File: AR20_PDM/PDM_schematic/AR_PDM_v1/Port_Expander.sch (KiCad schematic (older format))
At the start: 5 parts, among them U9 TCA6424ARGJR

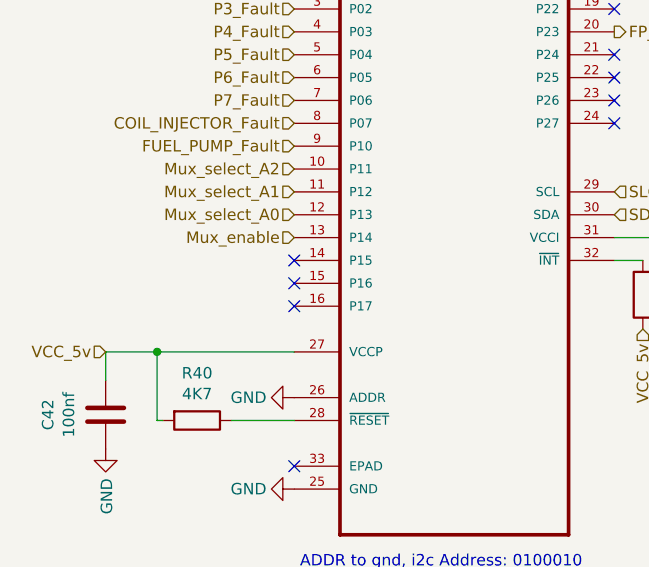
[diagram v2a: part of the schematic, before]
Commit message: Further testing, reveals pdm needs rework
-  As of now, there are major errors in schematics.
- Needs rework. Version charlie postponed.
- Very nice pcb layout thats almost finished. 
   worth noting this layout for the future
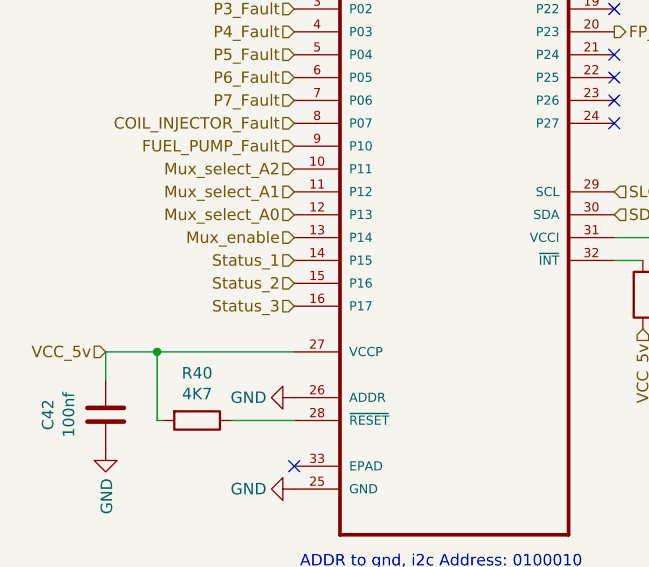
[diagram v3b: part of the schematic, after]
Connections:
- net Status_1: now reaches U9.14 (P15)
- net Status_2: now reaches U9.15 (P16)
- net Status_3: now reaches U9.16 (P17)
- no-connect marks 11 -> 8
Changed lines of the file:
@@
 	0    1    1    0
 $EndComp
+Text HLabel 6475 2950 2    50   Output ~ 0
+FP_ENABLE_ACM
+NoConn ~ 6475 2850
+NoConn ~ 6475 3050
+NoConn ~ 6475 3250
+NoConn ~ 6475 3150
+NoConn ~ 6475 3350
+Text HLabel 5075 3750 0    50   Input ~ 0
+Mux_select_A0
+Text HLabel 5075 3650 0    50   Input ~ 0
+Mux_select_A1
+Text HLabel 5075 3550 0    50   Input ~ 0
+Mux_select_A2
+Text HLabel 5075 3850 0    50   Input ~ 0
+Mux_enable
+Text HLabel 5075 3350 0    50   Input ~ 0
+COIL_INJECTOR_Fault
+Text HLabel 5075 3450 0    50   Input ~ 0
+FUEL_PUMP_Fault
+NoConn ~ 6475 2750
+NoConn ~ 6475 2650
+Text HLabel 5075 4050 0    50   Input ~ 0
+Status_2
+Text HLabel 5075 3950 0    50   Input ~ 0
+Status_1
+Text HLabel 5075 4150 0    50   Input ~ 0
+Status_3
 $Comp
 L AR20_PDM_v1-rescue:TCA6424ARGJR U9
@@
 	1    0    0    -1
 $EndComp
-Text HLabel 6475 2950 2    50   Output ~ 0
-FP_ENABLE_ACM
-NoConn ~ 6475 2850
-NoConn ~ 6475 3050
-NoConn ~ 6475 3250
-NoConn ~ 6475 3150
-NoConn ~ 6475 3350
-Text HLabel 5075 3750 0    50   Input ~ 0
-Mux_select_A0
-Text HLabel 5075 3650 0    50   Input ~ 0
-Mux_select_A1
-Text HLabel 5075 3550 0    50   Input ~ 0
-Mux_select_A2
-Text HLabel 5075 3850 0    50   Input ~ 0
-Mux_enable
-NoConn ~ 5075 3950
-NoConn ~ 5075 4050
-NoConn ~ 5075 4150
-Text HLabel 5075 3350 0    50   Input ~ 0
-COIL_INJECTOR_Fault
-Text HLabel 5075 3450 0    50   Input ~ 0
-FUEL_PUMP_Fault
-NoConn ~ 6475 2750
-NoConn ~ 6475 2650
 $EndSCHEMATC

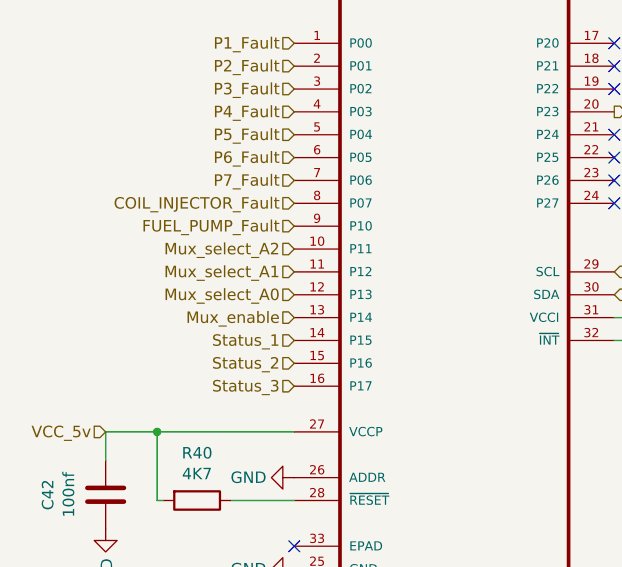
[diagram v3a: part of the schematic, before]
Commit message: schematics rework
Fixed INA233 frying due to inductive flyback:
- Paced ina233 high side of the mosftets
- New input protection reseistors, and zener diodes, on each ina233.
Simplified:
- Removed the MUX and mos sense lines, as i realize that most of this functionality can be obtained trough INA233.
- Removed some of the cappacitors , besides the most needed ones.
- removed  back to back zener diode configuration, now a single diode insted.
 to reduce negative voltage in case of loss of VS, to be easy on the INA233 filters.
new stuff:
- Another temp sensor.
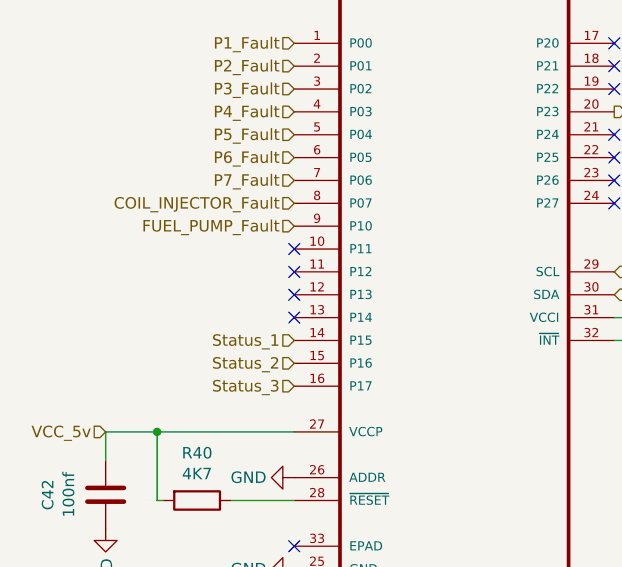
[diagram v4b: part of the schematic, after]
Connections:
- net Mux_enable: no longer names the net of U9.13 (P14)
- net Mux_select_A0: no longer names the net of U9.12 (P13)
- net Mux_select_A1: no longer names the net of U9.11 (P12)
- net Mux_select_A2: no longer names the net of U9.10 (P11)
- no-connect marks 8 -> 12
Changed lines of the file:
@@
 $Descr A4 11693 8268
 encoding utf-8
-Sheet 14 14
+Sheet 13 13
 Title ""
 Date ""
@@
 NoConn ~ 6475 3150
 NoConn ~ 6475 3350
-Text HLabel 5075 3750 0    50   Input ~ 0
-Mux_select_A0
-Text HLabel 5075 3650 0    50   Input ~ 0
-Mux_select_A1
-Text HLabel 5075 3550 0    50   Input ~ 0
-Mux_select_A2
-Text HLabel 5075 3850 0    50   Input ~ 0
-Mux_enable
 Text HLabel 5075 3350 0    50   Input ~ 0
 COIL_INJECTOR_Fault
@@
 	1    0    0    -1
 $EndComp
+NoConn ~ 5075 3550
+NoConn ~ 5075 3650
+NoConn ~ 5075 3750
+NoConn ~ 5075 3850
 $EndSCHEMATC

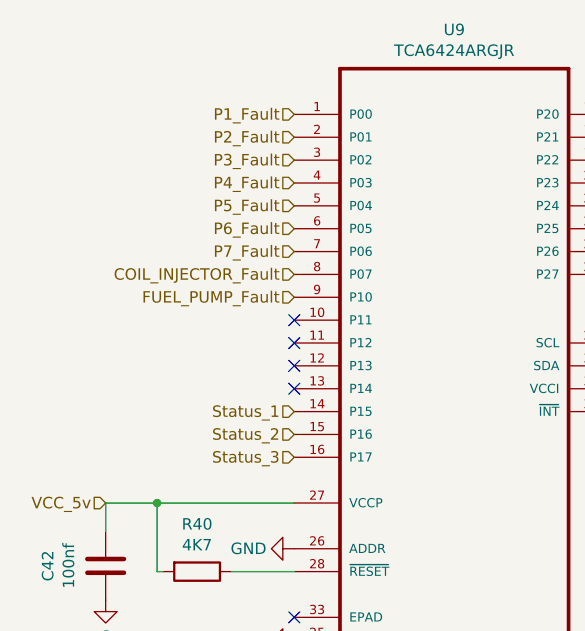
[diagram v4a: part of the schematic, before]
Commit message: PDM mostly complete
- Reverse polarity protection implemented
- All traces layed out
- final polish missing
- DRC missing
- Final check missing
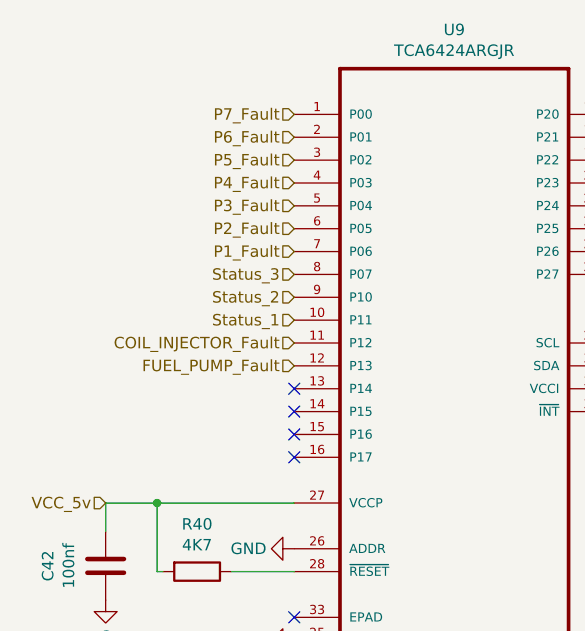
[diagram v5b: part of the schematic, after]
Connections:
- net COIL_INJECTOR_Fault: now also U9.11 (P12); no longer U9.8 (P07)
- net FUEL_PUMP_Fault: now also U9.12 (P13); no longer U9.9 (P10)
- net P1_Fault: now also U9.7 (P06); no longer U9.1 (P00)
- net P2_Fault: now also U9.6 (P05); no longer U9.2 (P01)
- net P3_Fault: now also U9.5 (P04); no longer U9.3 (P02)
- net P5_Fault: now also U9.3 (P02); no longer U9.5 (P04)
- net P6_Fault: now also U9.2 (P01); no longer U9.6 (P05)
- net P7_Fault: now also U9.1 (P00); no longer U9.7 (P06)
- net Status_1: now also U9.10 (P11); no longer U9.14 (P15)
- net Status_2: now also U9.9 (P10); no longer U9.15 (P16)
- net Status_3: now also U9.8 (P07); no longer U9.16 (P17)
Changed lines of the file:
@@
 	0    1    1    0
 $EndComp
-Text HLabel 5075 3250 0    50   Input ~ 0
+Text HLabel 5075 2650 0    50   Input ~ 0
 P7_Fault
-Text HLabel 5075 3150 0    50   Input ~ 0
+Text HLabel 5075 2750 0    50   Input ~ 0
 P6_Fault
-Text HLabel 5075 3050 0    50   Input ~ 0
+Text HLabel 5075 2850 0    50   Input ~ 0
 P5_Fault
 Text HLabel 5075 2950 0    50   Input ~ 0
 P4_Fault
-Text HLabel 5075 2850 0    50   Input ~ 0
+Text HLabel 5075 3050 0    50   Input ~ 0
 P3_Fault
-Text HLabel 5075 2650 0    50   Input ~ 0
+Text HLabel 5075 3250 0    50   Input ~ 0
 P1_Fault
-Text HLabel 5075 2750 0    50   Input ~ 0
+Text HLabel 5075 3150 0    50   Input ~ 0
 P2_Fault
 NoConn ~ 5075 4850
@@
 NoConn ~ 6475 3150
 NoConn ~ 6475 3350
-Text HLabel 5075 3350 0    50   Input ~ 0
-COIL_INJECTOR_Fault
-Text HLabel 5075 3450 0    50   Input ~ 0
-FUEL_PUMP_Fault
 NoConn ~ 6475 2750
 NoConn ~ 6475 2650
-Text HLabel 5075 4050 0    50   Input ~ 0
+Text HLabel 5075 3450 0    50   Input ~ 0
 Status_2
-Text HLabel 5075 3950 0    50   Input ~ 0
+Text HLabel 5075 3550 0    50   Input ~ 0
 Status_1
-Text HLabel 5075 4150 0    50   Input ~ 0
+Text HLabel 5075 3350 0    50   Input ~ 0
 Status_3
+NoConn ~ 5075 3950
+NoConn ~ 5075 3850
+NoConn ~ 5075 4150
+Text HLabel 5075 3750 0    50   Input ~ 0
+FUEL_PUMP_Fault
+Text HLabel 5075 3650 0    50   Input ~ 0
+COIL_INJECTOR_Fault
 $Comp
 L AR20_PDM_v1-rescue:TCA6424ARGJR U9
@@
 	1    0    0    -1
 $EndComp
-NoConn ~ 5075 3550
-NoConn ~ 5075 3650
-NoConn ~ 5075 3750
-NoConn ~ 5075 3850
+NoConn ~ 5075 4050
 $EndSCHEMATC

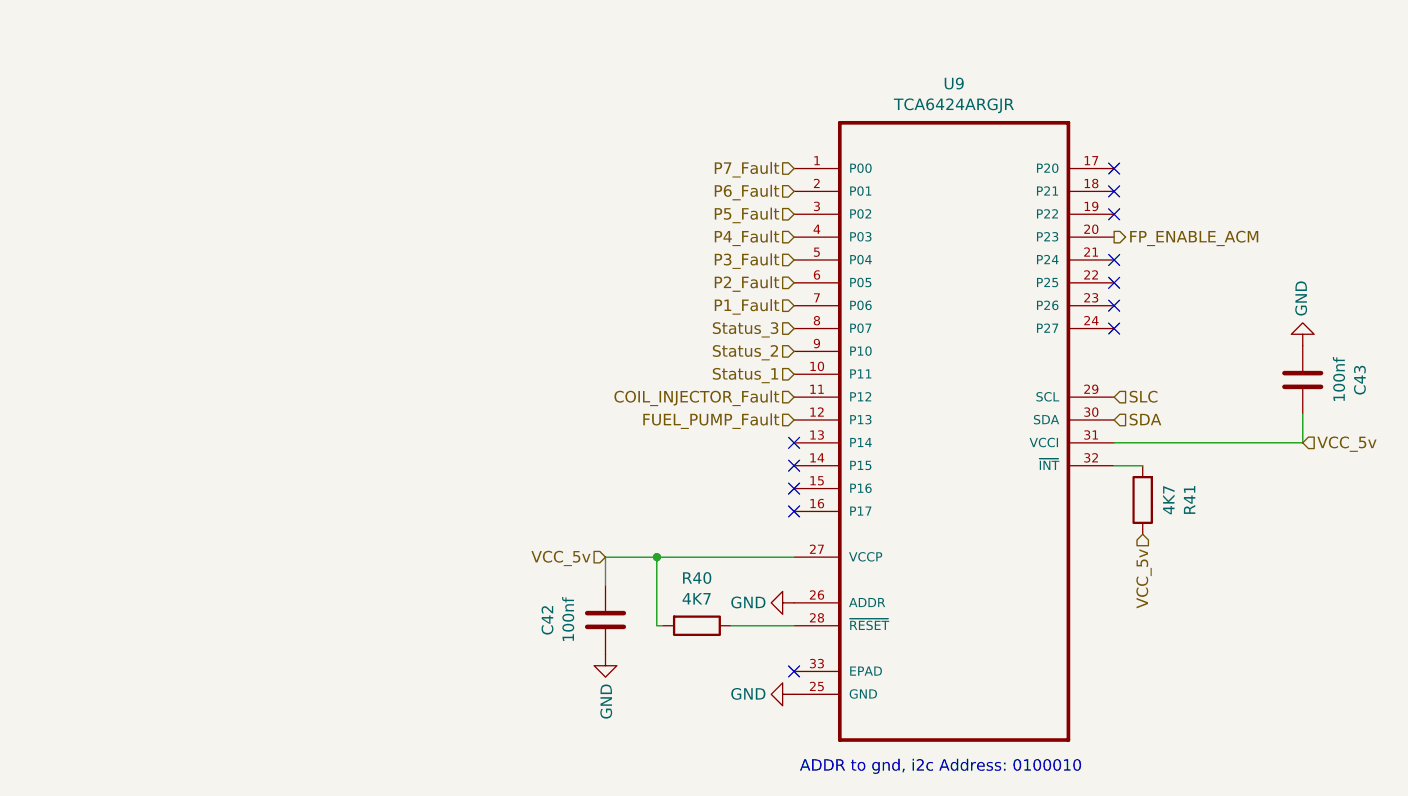
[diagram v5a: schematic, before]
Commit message: Added shutdown circuit monitoring, new gerber files
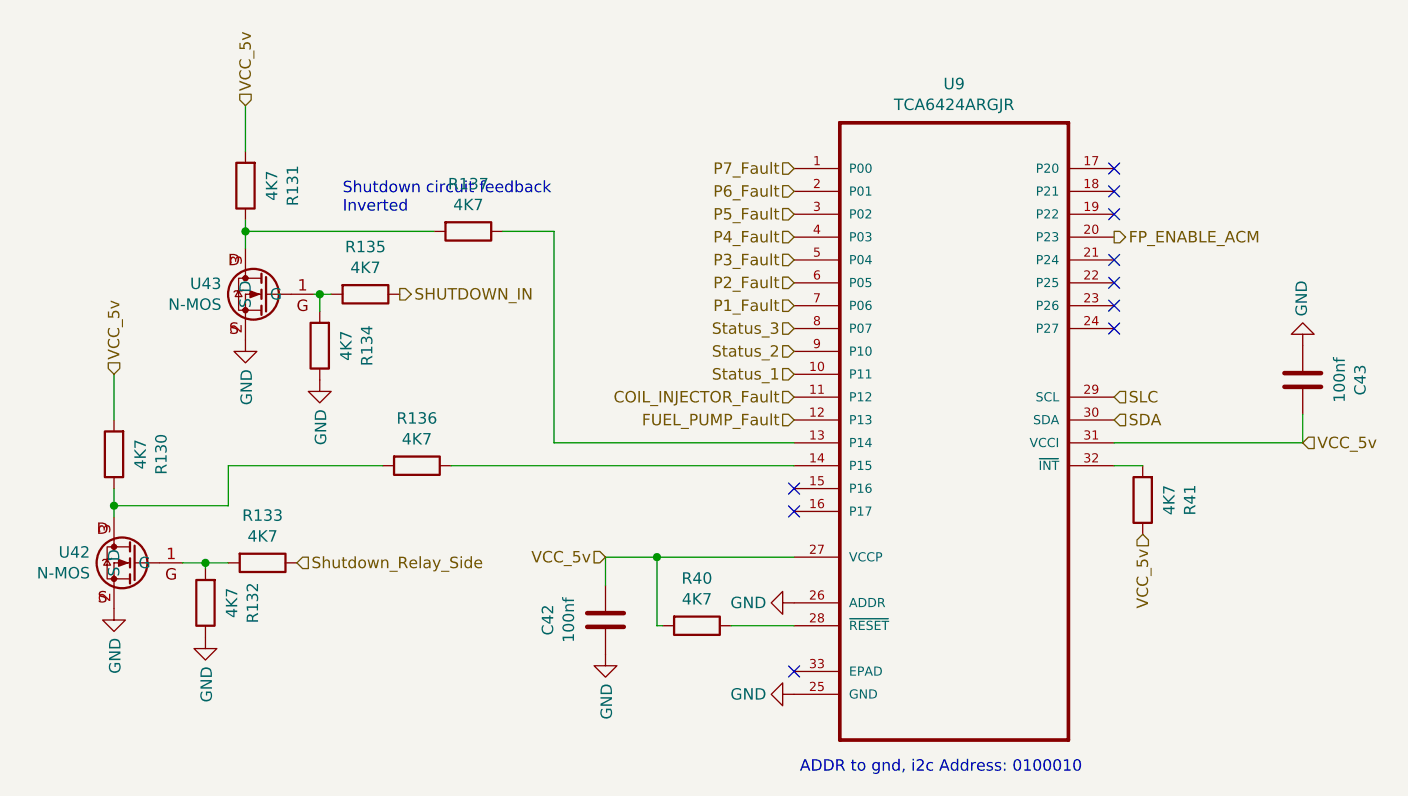
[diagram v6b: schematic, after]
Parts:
- added R130, R131, R132, R133, R134, R135, R136, R137: 4K7, Resistor_SMD:R_0603_1608Metric, symbol AR20_PDM_v1-rescue:R-Device
- added U42, U43: N-MOS, AR_PDM_v1:N-MOS-DMN6140L-13, symbol AR20_PDM_v1-rescue:N-MOS-DMN6140L-13
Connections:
- net GND: now also R132.1, R134.1, U42.2 (S), U43.2 (S)
- net VCC_5v: now also R130.2, R131.2
- net at U9.13 (P14): now also R137.1
- net at U9.14 (P15): now also R136.1
- new net: R132.2, R133.2, U42.1 (G)
- new net: R130.1, R136.2, U42.3 (D)
- new net: R134.2, R135.2, U43.1 (G)
- new net: R131.1, R137.2, U43.3 (D)
- new net SHUTDOWN_IN: R135.1
- new net Shutdown_Relay_Side: R133.1
- no-connect marks 12 -> 10
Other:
- note added: "Shutdown circuit feedback\nInverted"

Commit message: A litte fix in the shutdown monitoring, new gerber files
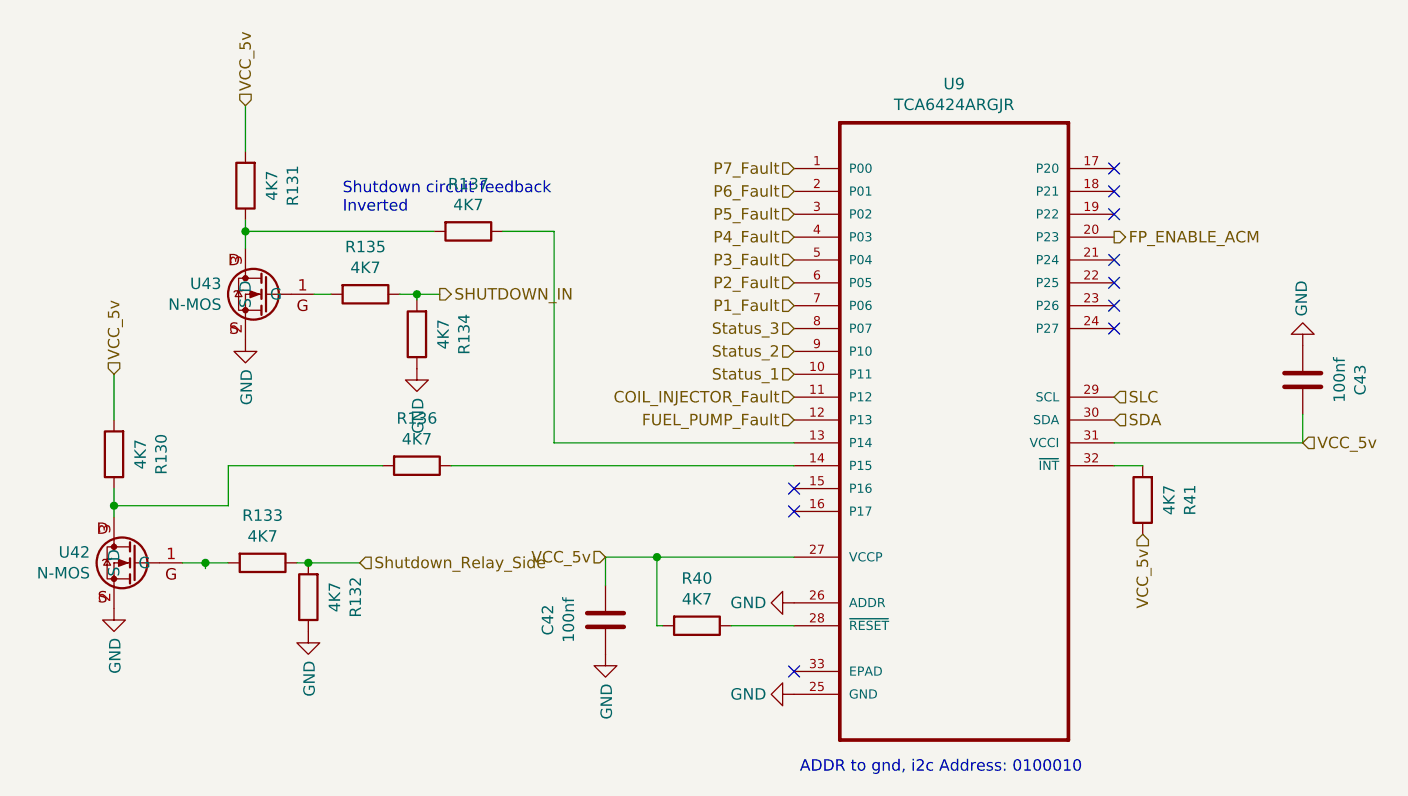
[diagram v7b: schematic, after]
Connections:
- wire segments 29 -> 32
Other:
- moved on the sheet: R132, R134
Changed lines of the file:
@@
 L AR20_PDM_v1-rescue:R-Device R?
 U 1 1 5F452FFA
-P 3000 3425
+P 3425 3375
 AR Path="/5DA89415/5F452FFA" Ref="R?"  Part="1"
 AR Path="/5DA8920B/5F452FFA" Ref="R?"  Part="1"
 AR Path="/5E2546F2/5F452FFA" Ref="R?"  Part="1"
 AR Path="/5E1AEC18/5F452FFA" Ref="R134"  Part="1"
-F 0 "R134" V 2793 3425 50  0000 C CNN
-F 1 "4K7" V 2884 3425 50  0000 C CNN
-F 2 "Resistor_SMD:R_0603_1608Metric" V 2930 3425 50  0001 C CNN
-F 3 "~" H 3000 3425 50  0001 C CNN
-	1    3000 3425
+F 0 "R134" V 3218 3375 50  0000 C CNN
+F 1 "4K7" V 3309 3375 50  0000 C CNN
+F 2 "Resistor_SMD:R_0603_1608Metric" V 3355 3375 50  0001 C CNN
+F 3 "~" H 3425 3375 50  0001 C CNN
+	1    3425 3375
 	-1   0    0    1
 $EndComp
@@
 	4025 3850 4025 2925
 Wire Wire Line
-	3050 3200 3000 3200
-Wire Wire Line
-	3000 3275 3000 3200
-Connection ~ 3000 3200
-Wire Wire Line
-	3000 3200 2975 3200
-Wire Wire Line
 	2100 4125 2100 4175
 Wire Wire Line
@@
 L AR20_PDM_v1-rescue:R-Device R?
 U 1 1 5F461877
-P 2500 4550
+P 2950 4525
 AR Path="/5DA89415/5F461877" Ref="R?"  Part="1"
 AR Path="/5DA8920B/5F461877" Ref="R?"  Part="1"
 AR Path="/5E2546F2/5F461877" Ref="R?"  Part="1"
 AR Path="/5E1AEC18/5F461877" Ref="R132"  Part="1"
-F 0 "R132" V 2293 4550 50  0000 C CNN
-F 1 "4K7" V 2384 4550 50  0000 C CNN
-F 2 "Resistor_SMD:R_0603_1608Metric" V 2430 4550 50  0001 C CNN
-F 3 "~" H 2500 4550 50  0001 C CNN
-	1    2500 4550
+F 0 "R132" V 2743 4525 50  0000 C CNN
+F 1 "4K7" V 2834 4525 50  0000 C CNN
+F 2 "Resistor_SMD:R_0603_1608Metric" V 2880 4525 50  0001 C CNN
+F 3 "~" H 2950 4525 50  0001 C CNN
+	1    2950 4525
 	-1   0    0    1
 $EndComp
@@
 L AR20_PDM_v1-rescue:GND-power #PWR?
 U 1 1 5F45F5EF
-P 3000 3575
+P 3425 3525
 AR Path="/5DA89415/5F45F5EF" Ref="#PWR?"  Part="1"
 AR Path="/5DEB10A1/5F45F5EF" Ref="#PWR?"  Part="1"
@@
 AR Path="/5E10174B/5F45F5EF" Ref="#PWR?"  Part="1"
 AR Path="/5E1AEC18/5F45F5EF" Ref="#PWR0172"  Part="1"
-F 0 "#PWR0172" H 3000 3325 50  0001 C CNN
-F 1 "GND" V 3005 3447 50  0000 R CNN
-F 2 "" H 3000 3575 50  0001 C CNN
-F 3 "" H 3000 3575 50  0001 C CNN
-	1    3000 3575
+F 0 "#PWR0172" H 3425 3275 50  0001 C CNN
+F 1 "GND" V 3430 3397 50  0000 R CNN
+F 2 "" H 3425 3525 50  0001 C CNN
+F 3 "" H 3425 3525 50  0001 C CNN
+	1    3425 3525
 	1    0    0    -1
 $EndComp
@@
 L AR20_PDM_v1-rescue:GND-power #PWR?
 U 1 1 5F4625C1
-P 2500 4700
+P 2950 4675
 AR Path="/5DA89415/5F4625C1" Ref="#PWR?"  Part="1"
 AR Path="/5DEB10A1/5F4625C1" Ref="#PWR?"  Part="1"
@@
 AR Path="/5E10174B/5F4625C1" Ref="#PWR?"  Part="1"
 AR Path="/5E1AEC18/5F4625C1" Ref="#PWR0173"  Part="1"
-F 0 "#PWR0173" H 2500 4450 50  0001 C CNN
-F 1 "GND" V 2505 4572 50  0000 R CNN
-F 2 "" H 2500 4700 50  0001 C CNN
-F 3 "" H 2500 4700 50  0001 C CNN
-	1    2500 4700
+F 0 "#PWR0173" H 2950 4425 50  0001 C CNN
+F 1 "GND" V 2955 4547 50  0000 R CNN
+F 2 "" H 2950 4675 50  0001 C CNN
+F 3 "" H 2950 4675 50  0001 C CNN
+	1    2950 4675
 	1    0    0    -1
 $EndComp
@@
 	2500 4375 2600 4375
 Connection ~ 2500 4375
-Text HLabel 3350 3200 2    50   Output ~ 0
+Text HLabel 3525 3200 2    50   Output ~ 0
 SHUTDOWN_IN
-Text HLabel 2900 4375 2    50   Input ~ 0
+Text HLabel 3175 4375 2    50   Input ~ 0
 Shutdown_Relay_Side
 Wire Wire Line
@@
 Wire Wire Line
 	2675 2925 2675 3000
+Wire Wire Line
+	2975 3200 3050 3200
+Wire Wire Line
+	3350 3200 3425 3200
+Wire Wire Line
+	3425 3200 3425 3225
+Wire Wire Line
+	3425 3200 3525 3200
+Connection ~ 3425 3200
+Wire Wire Line
+	2900 4375 2950 4375
+Wire Wire Line
+	2950 4375 3175 4375
+Connection ~ 2950 4375
 $EndSCHEMATC
